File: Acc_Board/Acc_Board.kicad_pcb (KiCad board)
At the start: 2 copper layers, 139.7 x 76.2 mm, 66 parts, among them J1 AIRs Power, J12 776087-1, J2 IsoSPI, J3 IMD BAT, J4 HV Power, J5 HVIL, J6 IMD, J7 Current Sensor, J8 Fans, J9 Shutdown IL, K1 Relay_SPST-NO, Q1 STS6NF20V, Q2 STS6NF20V, Q3 STS6NF20V, U1 ISO1050DUB, U10 DK1A1B-12V, U12 LTC6820, U15 MCP6004, U2 NUCLEO-L432KC, U3 DK1A1B-12V, U4 PQDE6W-Q110-S5-H-D, U5 R-78B5.0-2.0, U6 NSL-32, U7 DK1A1B-12V, U8 LM7809_TO220, U9 NSL-32

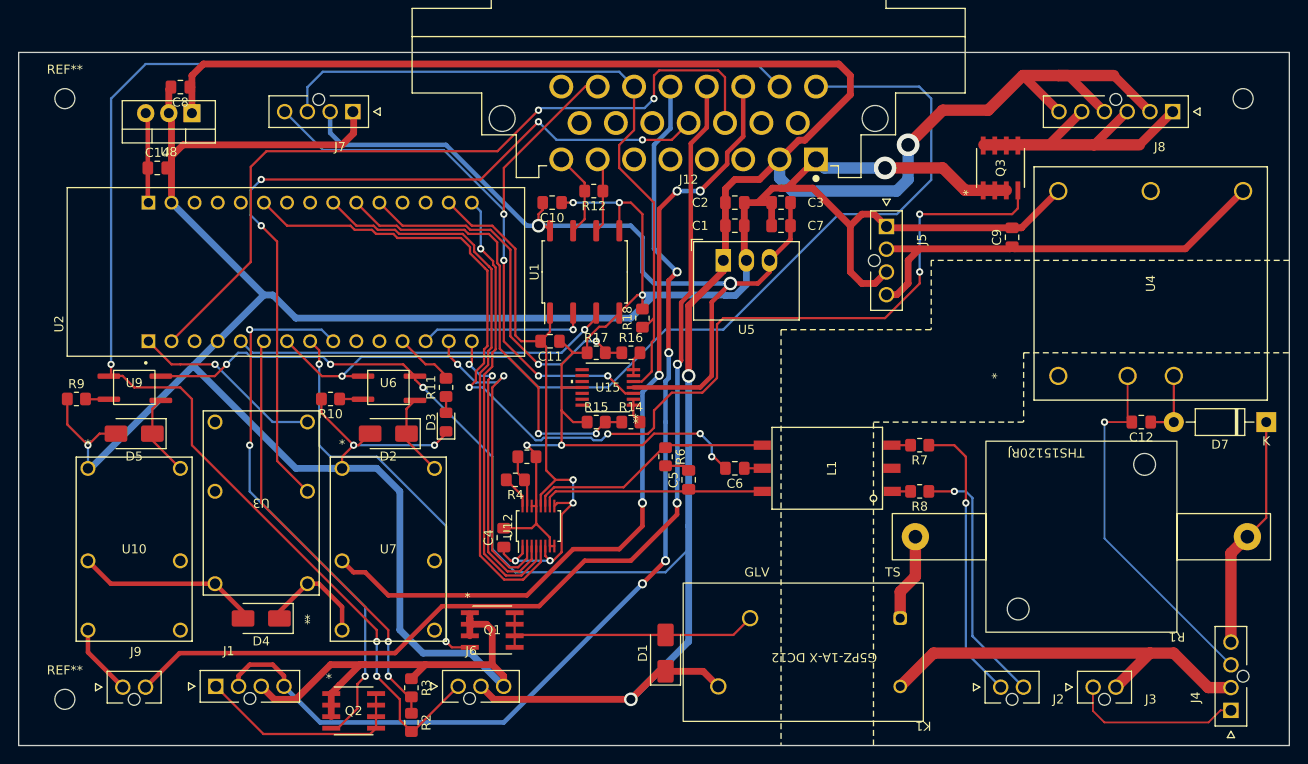
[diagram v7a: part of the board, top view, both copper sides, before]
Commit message: acc board All traces done and silkscreen improved
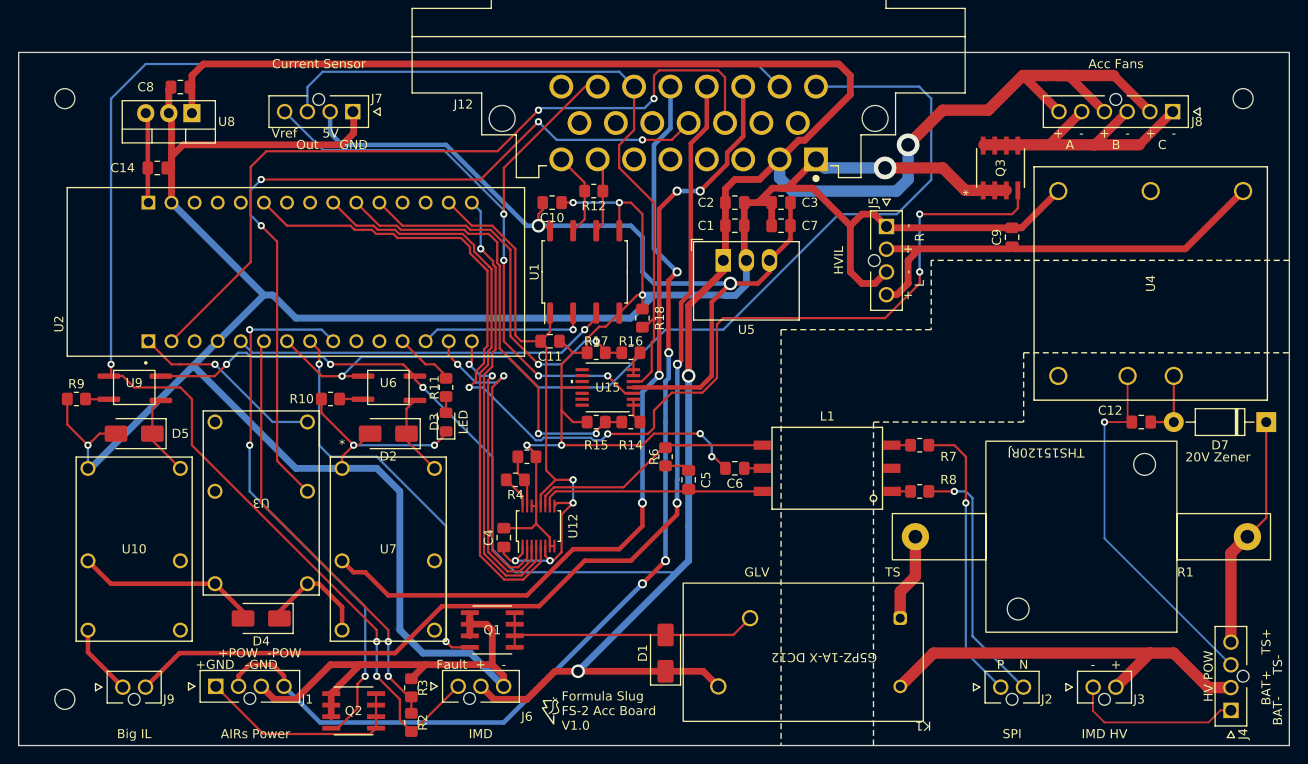
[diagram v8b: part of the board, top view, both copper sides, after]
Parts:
- added G***: LOGO, 1FS_2_Global_Footprint_Library:FORMULA SLUG, F.Cu at (74.3, 85.1)
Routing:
- net +12V: track 330.7 -> 326.9 mm
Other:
- board text added: "+"
- board text added: "+GND"
- board text added: "+POW"
- board text added: "-"
- board text added: "-GND"
- board text added: "-POW"
- board text added: "20V Zener"
- board text added: "5V"
- board text added: "A"
- board text added: "AIRs Power"
- board text added: "Acc Fans"
- board text added: "B"
- board text added: "BAT+"
- board text added: "BAT-"
- board text added: "Big IL"
- board text added: "C"
- board text added: "Current Sensor"
- board text added: "Fault"
- board text added: "Formula Slug FS-2 Acc Board V1.0"
- board text added: "GND"
- board text added: "HV POW"
- board text added: "HVIL"
- board text added: "IMD"
- board text added: "IMD HV"
- board text added: "L"
- board text added: "LED"
- board text added: "N"
- board text added: "Out"
- board text added: "P"
- board text added: "R"
- board text added: "SPI"
- board text added: "TS+"
- board text added: "TS-"
- board text added: "Vref"
